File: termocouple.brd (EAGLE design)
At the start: 69.8 x 100 mm, 21 parts, among them IC1 MAX31855, IC2 MAX31855, U2 TC1262_VDB, X2 1751248, X3 1751248

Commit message: Update termocouple.brd
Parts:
- moved X1 0.63 mm to (31.8, 88.9)
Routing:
- net N$8: track 70.5 -> 64.8 mm
- net N$15: track 64.3 -> 69.1 mm
- net N$9: track 76.8 -> 76.2 mm
- net N$5: track 70.5 -> 69.9 mm
- net N$12: track 85.7 -> 85.1 mm
- net N$11: track 80.6 -> 80.0 mm
- net +3V3: track 192.1 -> 191.5 mm
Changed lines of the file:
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@@
 <element name="IC1" library="adafruit" package="SO08" value="MAX31855" x="41.91" y="34.29"/>
 <element name="IC2" library="adafruit" package="SO08" value="MAX31855" x="58.42" y="34.29"/>
-<element name="X1" library="con-phoenix-254" package="10POL254" value="" x="31.75" y="89.535" rot="R180">
-<attribute name="OC_NEWARK" value="unknown" x="5.08" y="153.035" size="1.778" layer="27" rot="R180" display="off"/>
-<attribute name="MPN" value="" x="5.08" y="153.035" size="1.778" layer="27" rot="R180" display="off"/>
-<attribute name="MF" value="" x="5.08" y="153.035" size="1.778" layer="27" rot="R180" display="off"/>
-<attribute name="OC_FARNELL" value="unknown" x="5.08" y="153.035" size="1.778" layer="27" rot="R180" display="off"/>
+<element name="X1" library="con-phoenix-254" package="10POL254" value="" x="31.75" y="88.9" rot="R180">
+<attribute name="OC_NEWARK" value="unknown" x="5.08" y="152.4" size="1.778" layer="27" rot="R180" display="off"/>
+<attribute name="MPN" value="" x="5.08" y="152.4" size="1.778" layer="27" rot="R180" display="off"/>
+<attribute name="MF" value="" x="5.08" y="152.4" size="1.778" layer="27" rot="R180" display="off"/>
+<attribute name="OC_FARNELL" value="unknown" x="5.08" y="152.4" size="1.778" layer="27" rot="R180" display="off"/>
 </element>
 <element name="R43" library="rcl" package="R1206" value="10K" x="10.16" y="50.8" rot="R270"/>
@@
 <via x="8.255" y="60.96" extent="1-16" drill="0.6" shape="square"/>
 <wire x1="8.255" y1="60.96" x2="3.81" y2="60.96" width="0.6096" layer="1"/>
-<wire x1="43.18" y1="89.535" x2="54.61" y2="89.535" width="0.6096" layer="1"/>
-<wire x1="54.61" y1="89.535" x2="54.61" y2="60.96" width="0.6096" layer="1"/>
+<wire x1="43.18" y1="88.9" x2="54.61" y2="88.9" width="0.6096" layer="1"/>
+<wire x1="54.61" y1="88.9" x2="54.61" y2="60.96" width="0.6096" layer="1"/>
 <via x="54.61" y="60.96" extent="1-16" drill="0.6" shape="square"/>
 <contactref element="C1" pad="1"/>
@@
 <via x="23.495" y="81.915" extent="1-16" drill="0.6" shape="square"/>
 <wire x1="23.495" y1="81.915" x2="38.1" y2="81.915" width="0.4064" layer="16"/>
-<wire x1="38.1" y1="81.915" x2="38.1" y2="89.535" width="0.4064" layer="16"/>
+<wire x1="38.1" y1="81.915" x2="38.1" y2="88.9" width="0.4064" layer="16"/>
 </signal>
 <signal name="N$8">
 <contactref element="U$1" pad="SCL"/>
 <contactref element="X1" pad="4"/>
-<wire x1="35.56" y1="89.535" x2="35.56" y2="84.455" width="0.4064" layer="16"/>
-<wire x1="35.56" y1="84.455" x2="19.685" y2="84.455" width="0.4064" layer="16"/>
-<via x="19.685" y="84.455" extent="1-16" drill="0.6" shape="square"/>
-<wire x1="19.685" y1="84.455" x2="22.225" y2="84.455" width="0.4064" layer="1"/>
+<wire x1="35.56" y1="88.9" x2="35.56" y2="84.455" width="0.4064" layer="16"/>
+<wire x1="35.56" y1="84.455" x2="22.225" y2="84.455" width="0.4064" layer="16"/>
+<via x="22.225" y="84.455" extent="1-16" drill="0.6" shape="square"/>
 <wire x1="22.225" y1="84.455" x2="22.225" y2="50.165" width="0.4064" layer="1"/>
 <wire x1="22.225" y1="50.165" x2="15.24" y2="50.165" width="0.4064" layer="1"/>
@@
 <contactref element="X1" pad="5"/>
 <wire x1="30.48" y1="19.05" x2="28.575" y2="19.05" width="0.4064" layer="16"/>
-<wire x1="28.575" y1="19.05" x2="28.575" y2="52.705" width="0.4064" layer="16"/>
-<via x="28.575" y="52.705" extent="1-16" drill="0.6" shape="square"/>
-<wire x1="28.575" y1="52.705" x2="33.02" y2="52.705" width="0.4064" layer="1"/>
-<wire x1="33.02" y1="52.705" x2="33.02" y2="89.535" width="0.4064" layer="1"/>
+<wire x1="28.575" y1="19.05" x2="28.575" y2="53.34" width="0.4064" layer="16"/>
+<via x="28.575" y="53.34" extent="1-16" drill="0.6" shape="square"/>
+<wire x1="28.575" y1="53.34" x2="33.02" y2="53.34" width="0.4064" layer="1"/>
+<wire x1="33.02" y1="53.34" x2="33.02" y2="88.9" width="0.4064" layer="1"/>
 </signal>
 <signal name="N$10">
@@
 <via x="26.67" y="55.88" extent="1-16" drill="0.6" shape="square"/>
 <wire x1="26.67" y1="55.88" x2="27.94" y2="55.88" width="0.4064" layer="1"/>
-<wire x1="27.94" y1="55.88" x2="27.94" y2="89.535" width="0.4064" layer="1"/>
+<wire x1="27.94" y1="55.88" x2="27.94" y2="88.9" width="0.4064" layer="1"/>
 </signal>
 <signal name="N$12">
@@
 <wire x1="25.4" y1="46.355" x2="25.4" y2="58.42" width="0.4064" layer="16"/>
 <via x="25.4" y="58.42" extent="1-16" drill="0.6" shape="square"/>
-<wire x1="25.4" y1="58.42" x2="25.4" y2="89.535" width="0.4064" layer="1"/>
+<wire x1="25.4" y1="58.42" x2="25.4" y2="88.9" width="0.4064" layer="1"/>
 </signal>
 <signal name="N$22">
@@
 <contactref element="SV1" pad="4"/>
 <contactref element="U$1" pad="D2"/>
-<wire x1="30.48" y1="8.89" x2="29.21" y2="8.89" width="0.4064" layer="1"/>
-<wire x1="49.53" y1="48.26" x2="49.53" y2="50.165" width="0.4064" layer="1"/>
-<wire x1="49.53" y1="50.165" x2="48.895" y2="50.8" width="0.4064" layer="1"/>
-<wire x1="48.895" y1="50.8" x2="45.72" y2="50.8" width="0.4064" layer="1"/>
-<wire x1="45.72" y1="50.8" x2="45.085" y2="50.165" width="0.4064" layer="1"/>
-<wire x1="45.085" y1="50.165" x2="45.085" y2="44.45" width="0.4064" layer="1"/>
-<wire x1="45.085" y1="44.45" x2="44.45" y2="43.815" width="0.4064" layer="1"/>
-<wire x1="44.45" y1="43.815" x2="35.56" y2="43.815" width="0.4064" layer="1"/>
-<wire x1="35.56" y1="43.815" x2="34.29" y2="42.545" width="0.4064" layer="1"/>
-<wire x1="34.29" y1="42.545" x2="34.29" y2="38.735" width="0.4064" layer="1"/>
-<wire x1="34.29" y1="38.735" x2="33.655" y2="38.1" width="0.4064" layer="1"/>
-<wire x1="33.655" y1="38.1" x2="29.21" y2="38.1" width="0.4064" layer="1"/>
-<wire x1="29.21" y1="38.1" x2="28.575" y2="37.465" width="0.4064" layer="1"/>
-<wire x1="28.575" y1="37.465" x2="28.575" y2="9.525" width="0.4064" layer="1"/>
-<wire x1="28.575" y1="9.525" x2="29.21" y2="8.89" width="0.4064" layer="1"/>
+<wire x1="30.48" y1="8.89" x2="27.94" y2="8.89" width="0.4064" layer="1"/>
+<wire x1="27.94" y1="8.89" x2="27.94" y2="51.435" width="0.4064" layer="1"/>
+<wire x1="27.94" y1="51.435" x2="48.26" y2="51.435" width="0.4064" layer="1"/>
+<wire x1="48.26" y1="51.435" x2="49.53" y2="50.165" width="0.4064" layer="1"/>
+<wire x1="49.53" y1="50.165" x2="49.53" y2="48.26" width="0.4064" layer="1"/>
 </signal>
 </signals>

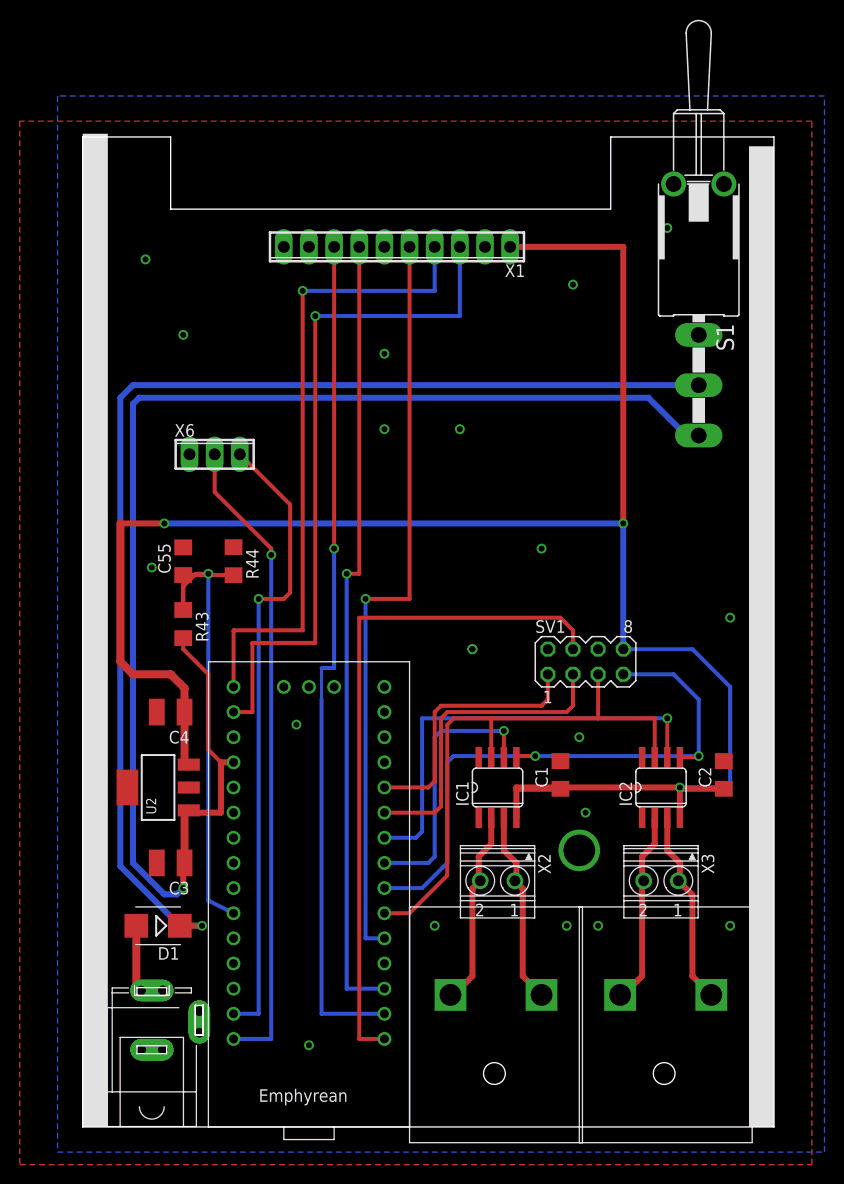
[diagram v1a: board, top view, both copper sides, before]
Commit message: update display.brd and thermocouple
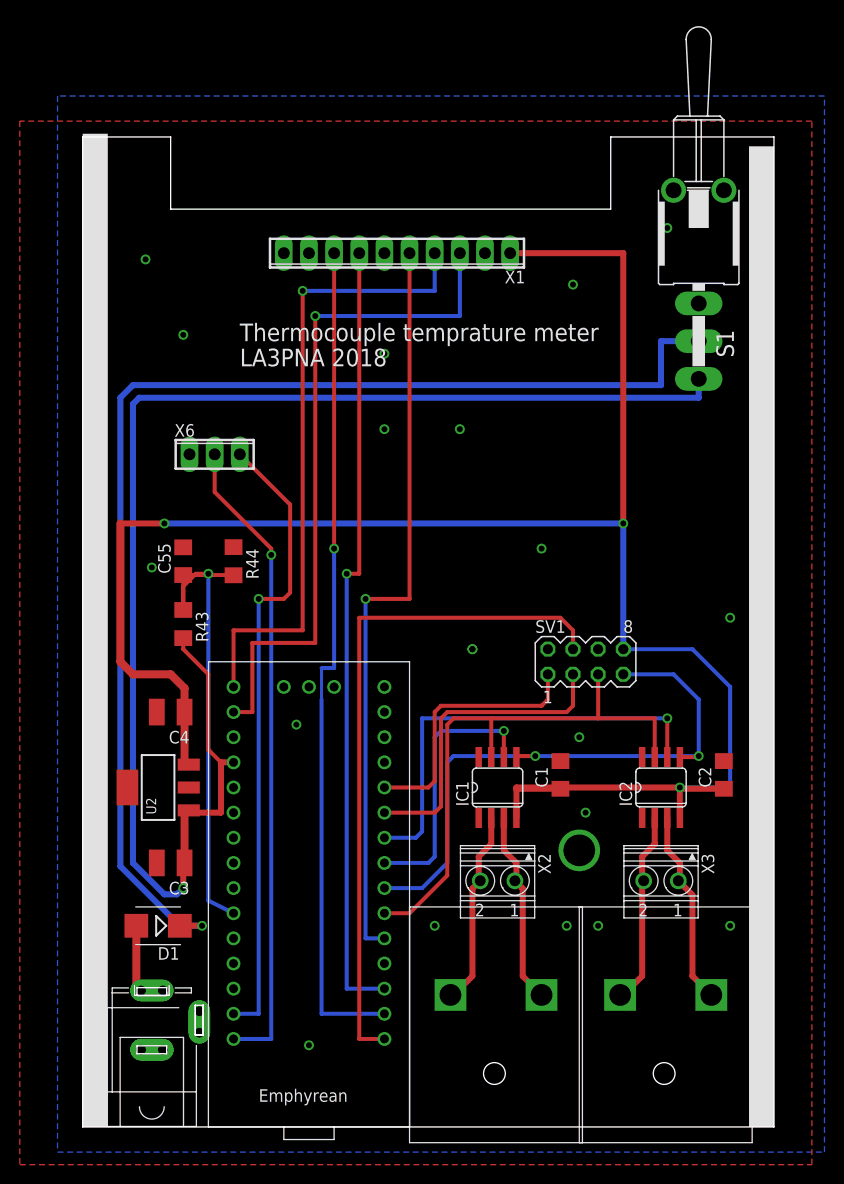
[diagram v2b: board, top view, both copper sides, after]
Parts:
- moved S1 0.64 mm to (62.2, 94.6)
- moved X1 0.64 mm to (31.8, 88.3)
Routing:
- net N$13: track 119.3 -> 123.7 mm
- net N$8: track 64.8 -> 64.1 mm
- net N$9: track 76.2 -> 75.6 mm
- net N$5: track 69.9 -> 69.2 mm
- net N$12: track 85.1 -> 84.5 mm
- net N$11: track 80.0 -> 79.4 mm
- net +3V3: track 191.5 -> 190.9 mm
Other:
- board text added: "LA3PNA 2018"
- board text added: "Thermocouple temprature meter"
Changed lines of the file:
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@@
 <dimension x1="53.34" y1="92.71" x2="8.89" y2="92.71" x3="31.115" y3="107.315" textsize="1.778" layer="21"/>
 <dimension x1="8.89" y1="92.71" x2="31.75" y2="92.71" x3="20.32" y3="90.805" textsize="1.778" layer="21"/>
+<text x="15.875" y="79.375" size="1.778" layer="25">Thermocouple temprature meter</text>
+<text x="15.875" y="76.835" size="1.778" layer="25">LA3PNA 2018</text>
 </plain>
 <attributes>
@@
 <element name="IC1" library="adafruit" package="SO08" value="MAX31855" x="41.91" y="34.29"/>
 <element name="IC2" library="adafruit" package="SO08" value="MAX31855" x="58.42" y="34.29"/>
-<element name="X1" library="con-phoenix-254" package="10POL254" value="" x="31.75" y="88.9" rot="R180">
-<attribute name="OC_NEWARK" value="unknown" x="5.08" y="152.4" size="1.778" layer="27" rot="R180" display="off"/>
-<attribute name="MPN" value="" x="5.08" y="152.4" size="1.778" layer="27" rot="R180" display="off"/>
-<attribute name="MF" value="" x="5.08" y="152.4" size="1.778" layer="27" rot="R180" display="off"/>
-<attribute name="OC_FARNELL" value="unknown" x="5.08" y="152.4" size="1.778" layer="27" rot="R180" display="off"/>
+<element name="X1" library="con-phoenix-254" package="10POL254" value="" x="31.75" y="88.265" rot="R180">
+<attribute name="OC_NEWARK" value="unknown" x="5.08" y="151.765" size="1.778" layer="27" rot="R180" display="off"/>
+<attribute name="MPN" value="" x="5.08" y="151.765" size="1.778" layer="27" rot="R180" display="off"/>
+<attribute name="MF" value="" x="5.08" y="151.765" size="1.778" layer="27" rot="R180" display="off"/>
+<attribute name="OC_FARNELL" value="unknown" x="5.08" y="151.765" size="1.778" layer="27" rot="R180" display="off"/>
 </element>
 <element name="R43" library="rcl" package="R1206" value="10K" x="10.16" y="50.8" rot="R270"/>
@@
 <element name="C4" library="rcl" package="C1210" value="10u (1210)" x="8.89" y="41.91" rot="R180"/>
 <element name="J2" library="PI Teensy" package="SPC4078" value="" x="6.985" y="10.795" rot="R90"/>
-<element name="S1" library="switch" package="LPV-1" value="" x="62.23" y="95.25" rot="R180"/>
+<element name="S1" library="switch" package="LPV-1" value="" x="62.23" y="94.615" rot="R180"/>
 <element name="D1" library="diode" package="SMB" value="VS-10BQ015-M3" x="7.62" y="20.32" rot="R180"/>
 <element name="X2" library="con-phoenix-350" package="1751248" value="1751248" x="41.91" y="24.765" rot="R180">
@@
 <via x="8.255" y="60.96" extent="1-16" drill="0.6" shape="square"/>
 <wire x1="8.255" y1="60.96" x2="3.81" y2="60.96" width="0.6096" layer="1"/>
-<wire x1="43.18" y1="88.9" x2="54.61" y2="88.9" width="0.6096" layer="1"/>
-<wire x1="54.61" y1="88.9" x2="54.61" y2="60.96" width="0.6096" layer="1"/>
+<wire x1="43.18" y1="88.265" x2="54.61" y2="88.265" width="0.6096" layer="1"/>
+<wire x1="54.61" y1="88.265" x2="54.61" y2="60.96" width="0.6096" layer="1"/>
 <via x="54.61" y="60.96" extent="1-16" drill="0.6" shape="square"/>
 <contactref element="C1" pad="1"/>
@@
 <wire x1="12.7" y1="45.72" x2="12.7" y2="38.1" width="0.4064" layer="1"/>
 <wire x1="12.7" y1="38.1" x2="13.97" y2="36.83" width="0.4064" layer="1"/>
-<wire x1="62.23" y1="69.85" x2="60.96" y2="69.85" width="0.6096" layer="16"/>
-<wire x1="60.96" y1="69.85" x2="57.15" y2="73.66" width="0.6096" layer="16"/>
-<wire x1="57.15" y1="73.66" x2="5.715" y2="73.66" width="0.6096" layer="16"/>
+<wire x1="62.23" y1="75.565" x2="62.23" y2="73.66" width="0.6096" layer="16"/>
+<wire x1="62.23" y1="73.66" x2="5.715" y2="73.66" width="0.6096" layer="16"/>
 <wire x1="5.715" y1="73.66" x2="5.08" y2="73.025" width="0.6096" layer="16"/>
 <wire x1="5.08" y1="73.025" x2="5.08" y2="26.67" width="0.6096" layer="16"/>
@@
 <via x="23.495" y="81.915" extent="1-16" drill="0.6" shape="square"/>
 <wire x1="23.495" y1="81.915" x2="38.1" y2="81.915" width="0.4064" layer="16"/>
-<wire x1="38.1" y1="81.915" x2="38.1" y2="88.9" width="0.4064" layer="16"/>
+<wire x1="38.1" y1="81.915" x2="38.1" y2="88.265" width="0.4064" layer="16"/>
 </signal>
 <signal name="N$8">
 <contactref element="U$1" pad="SCL"/>
 <contactref element="X1" pad="4"/>
-<wire x1="35.56" y1="88.9" x2="35.56" y2="84.455" width="0.4064" layer="16"/>
+<wire x1="35.56" y1="88.265" x2="35.56" y2="84.455" width="0.4064" layer="16"/>
 <wire x1="35.56" y1="84.455" x2="22.225" y2="84.455" width="0.4064" layer="16"/>
 <via x="22.225" y="84.455" extent="1-16" drill="0.6" shape="square"/>
@@
 <contactref element="S1" pad="2"/>
 <contactref element="D1" pad="C"/>
-<wire x1="62.23" y1="74.93" x2="5.08" y2="74.93" width="0.6096" layer="16"/>
+<wire x1="62.23" y1="79.375" x2="58.42" y2="79.375" width="0.6096" layer="16"/>
+<wire x1="58.42" y1="79.375" x2="58.42" y2="74.93" width="0.6096" layer="16"/>
+<wire x1="58.42" y1="74.93" x2="5.08" y2="74.93" width="0.6096" layer="16"/>
 <wire x1="5.08" y1="74.93" x2="3.81" y2="73.66" width="0.6096" layer="16"/>
 <wire x1="3.81" y1="73.66" x2="3.81" y2="26.33" width="0.6096" layer="16"/>
@@
 <via x="28.575" y="53.34" extent="1-16" drill="0.6" shape="square"/>
 <wire x1="28.575" y1="53.34" x2="33.02" y2="53.34" width="0.4064" layer="1"/>
-<wire x1="33.02" y1="53.34" x2="33.02" y2="88.9" width="0.4064" layer="1"/>
+<wire x1="33.02" y1="53.34" x2="33.02" y2="88.265" width="0.4064" layer="1"/>
 </signal>
 <signal name="N$10">
@@
 <via x="26.67" y="55.88" extent="1-16" drill="0.6" shape="square"/>
 <wire x1="26.67" y1="55.88" x2="27.94" y2="55.88" width="0.4064" layer="1"/>
-<wire x1="27.94" y1="55.88" x2="27.94" y2="88.9" width="0.4064" layer="1"/>
+<wire x1="27.94" y1="55.88" x2="27.94" y2="88.265" width="0.4064" layer="1"/>
 </signal>
 <signal name="N$12">
@@
 <wire x1="25.4" y1="46.355" x2="25.4" y2="58.42" width="0.4064" layer="16"/>
 <via x="25.4" y="58.42" extent="1-16" drill="0.6" shape="square"/>
-<wire x1="25.4" y1="58.42" x2="25.4" y2="88.9" width="0.4064" layer="1"/>
+<wire x1="25.4" y1="58.42" x2="25.4" y2="88.265" width="0.4064" layer="1"/>
 </signal>
 <signal name="N$22">

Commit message: pcb add fiducials
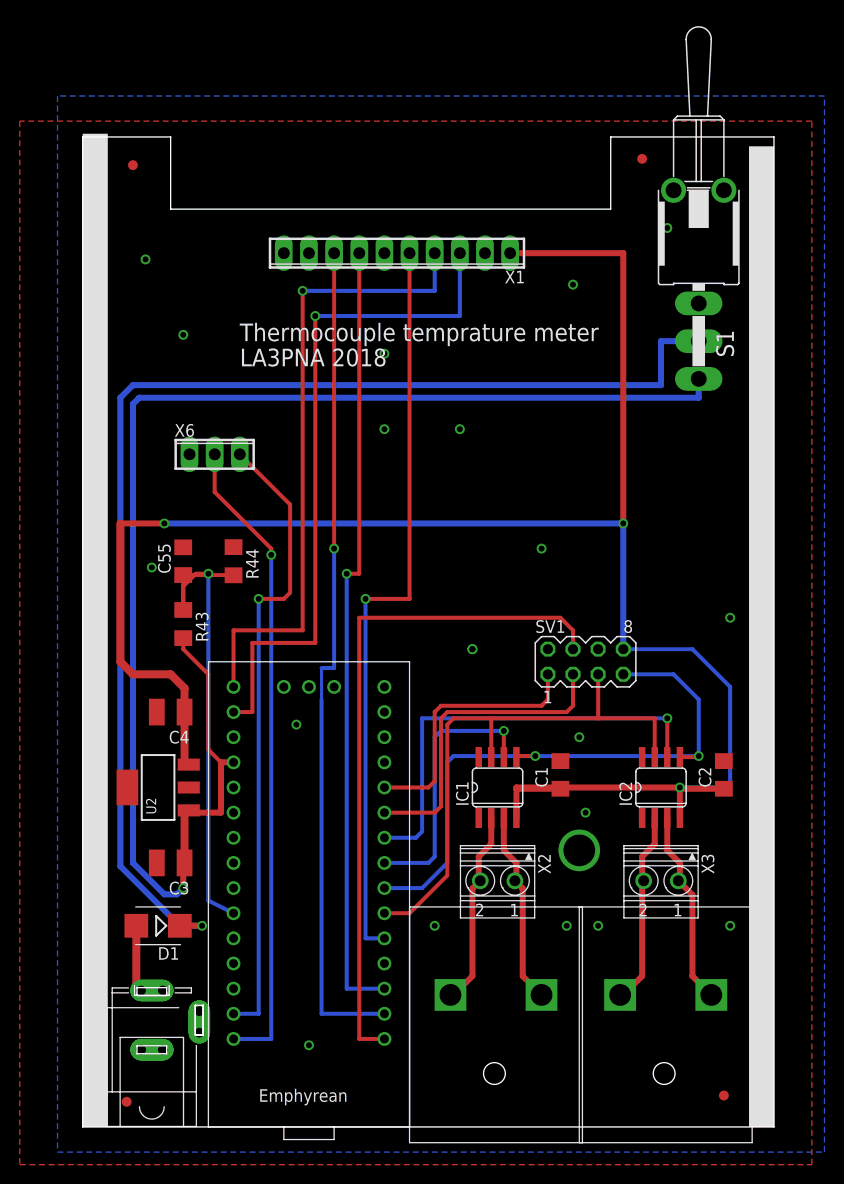
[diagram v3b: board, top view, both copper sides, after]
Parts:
- added U$4, U$5, U$6, U$7: FIDUCIAL, tracker:FIDUCIAL_1MM
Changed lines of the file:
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@@
 </class>
 </classes>
-<designrules name="default">
+<designrules name="default *">
 <description language="de">&lt;b&gt;EAGLE Design Rules&lt;/b&gt;
 &lt;p&gt;
@@
 <param name="mlMinCreamFrame" value="0mil"/>
 <param name="mlMaxCreamFrame" value="0mil"/>
-<param name="mlViaStopLimit" value="0mil"/>
+<param name="mlViaStopLimit" value="0.7mm"/>
 <param name="srRoundness" value="0"/>
 <param name="srMinRoundness" value="0mil"/>
@@
 <element name="C1" library="rcl" package="C1206" value="100n" x="48.26" y="35.56" rot="R90"/>
 <element name="C2" library="rcl" package="C1206" value="100n" x="64.77" y="35.56" rot="R90"/>
+<element name="U$4" library="tracker" package="FIDUCIAL_1MM" value="FIDUCIAL" x="5.08" y="97.155"/>
+<element name="U$5" library="tracker" package="FIDUCIAL_1MM" value="FIDUCIAL" x="64.77" y="3.175"/>
+<element name="U$6" library="tracker" package="FIDUCIAL_1MM" value="FIDUCIAL" x="56.515" y="97.79"/>
+<element name="U$7" library="tracker" package="FIDUCIAL_1MM" value="FIDUCIAL" x="4.445" y="2.54"/>
 </elements>
 <signals>
